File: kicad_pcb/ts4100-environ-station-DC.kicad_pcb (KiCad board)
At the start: 2 copper layers, 95 x 57.8 mm, 22 parts, among them CN1 Conn_02x08_Odd_Even, CN2 LXD-M4492C-LCD, CN3 Conn_01x02_MountingPin, CN4 Conn_01x04, Q1 DMN65D8LDW, U1 MS860702BA01-50

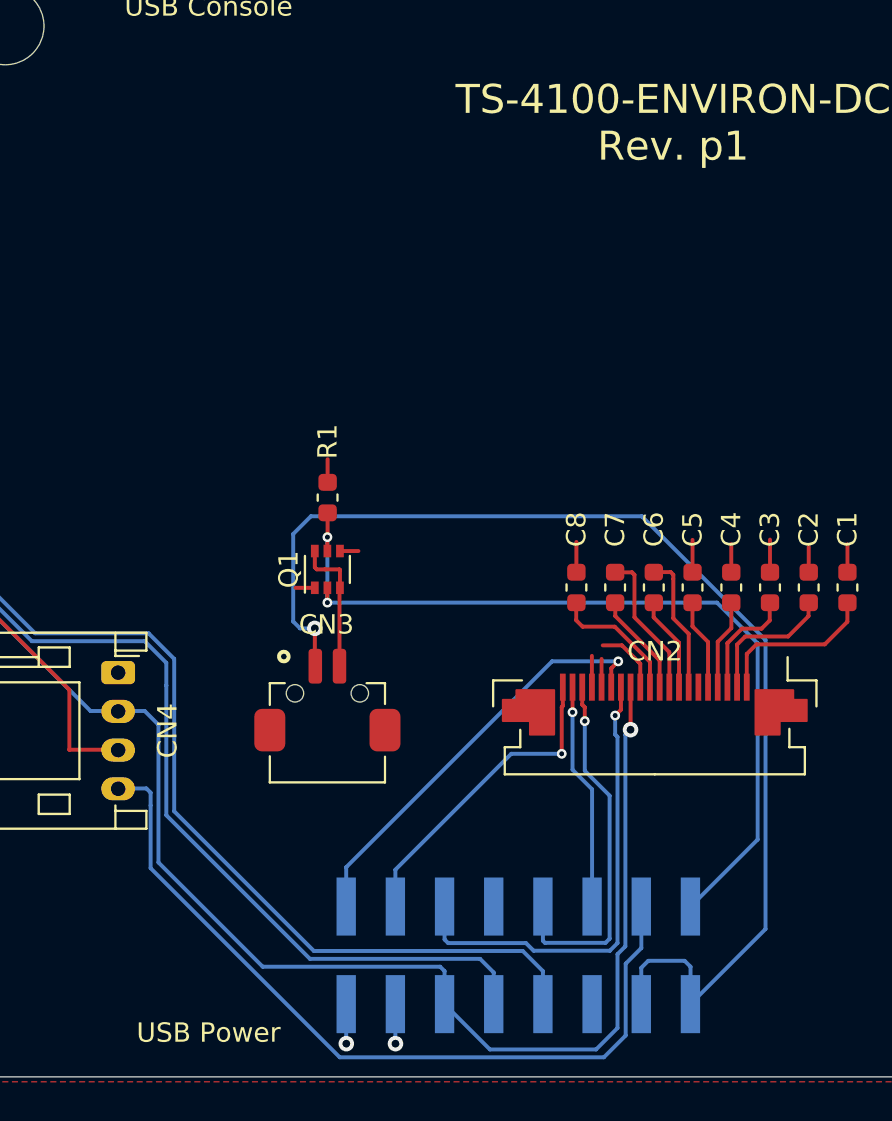
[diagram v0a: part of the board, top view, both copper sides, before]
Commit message: kicad_pcb: Bump to PCB rev p2
Runs LCD backlight on 3.3 V instead of 5 V, update silk, adds gnd
to backlight connector mounting pad footprints for mechanical
stability
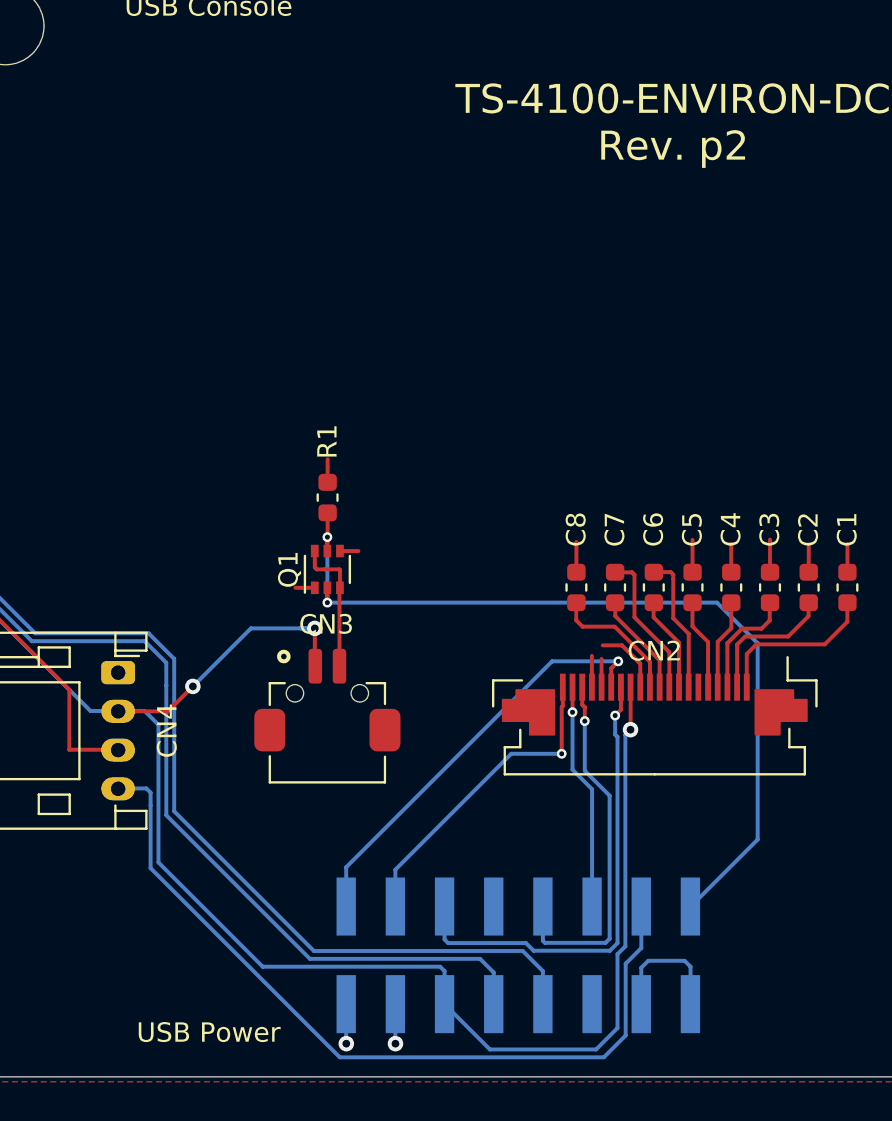
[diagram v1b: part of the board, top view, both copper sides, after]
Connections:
- CN3 pad 1: +5V -> +3V3
- CN3 pad MP: Net-(CN3-PadMP) -> GND
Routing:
- net +5V: track 62.1 -> 6.63 mm, vias 1 -> 0
- net +3V3: track 96.0 -> 110.5 mm, vias 2 -> 4
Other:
- board text added: "TS-4100-ENVIRON-DC Rev. p2"
- board text removed: "TS-4100-ENVIRON-DC Rev. p1"
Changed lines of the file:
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@@
     (thickness 1.6)
     (drawings 35)
-    (tracks 224)
+    (tracks 223)
     (zones 0)
     (modules 22)
-    (nets 35)
+    (nets 34)
   )
   (page A)
@@
     (mod_text_size 1 1)
     (mod_text_width 0.15)
-    (pad_size 1.7 1.7)
-    (pad_drill 1)
+    (pad_size 1.6 2.2)
+    (pad_drill 0)
     (pad_to_mask_clearance 0.05)
     (aux_axis_origin 0 0)
@@
   (net 31 "Net-(CN2-Pad21)")
   (net 32 "Net-(CN3-Pad2)")
-  (net 33 "Net-(CN3-PadMP)")
-  (net 34 "Net-(CN4-Pad1)")
+  (net 33 "Net-(CN4-Pad1)")
   (net_class Default "This is the default net class."
     (clearance 0.2032)
@@
     (add_net "Net-(CN2-Pad6)")
     (add_net "Net-(CN3-Pad2)")
-    (add_net "Net-(CN3-PadMP)")
     (add_net "Net-(CN4-Pad1)")
     (add_net "Net-(U1-Pad2)")
@@
     (fp_circle (center -2.25 -0.5) (end -2.15 -0.5) (layer F.SilkS) (width 0.5))
     (pad 1 smd roundrect (at -0.625 0) (size 0.7 1.8) (layers F.Cu F.Paste F.Mask) (roundrect_rratio 0.25)
-      (net 19 +5V))
+      (net 11 +3V3))
     (pad 2 smd roundrect (at 0.625 0) (size 0.7 1.8) (layers F.Cu F.Paste F.Mask) (roundrect_rratio 0.25)
       (net 32 "Net-(CN3-Pad2)"))
     (pad MP smd roundrect (at -2.975 3.3) (size 1.6 2.2) (layers F.Cu F.Paste F.Mask) (roundrect_rratio 0.25)
-      (net 33 "Net-(CN3-PadMP)"))
+      (net 1 GND))
     (pad MP smd roundrect (at 2.975 3.3) (size 1.6 2.2) (layers F.Cu F.Paste F.Mask) (roundrect_rratio 0.25)
-      (net 33 "Net-(CN3-PadMP)"))
+      (net 1 GND))
     (pad "" np_thru_hole circle (at 1.675 1.4) (size 0.9 0.9) (drill 0.9) (layers *.Cu *.Mask))
     (pad "" np_thru_hole circle (at -1.675 1.4) (size 0.9 0.9) (drill 0.9) (layers *.Cu *.Mask))
@@
     )
     (pad 1 thru_hole roundrect (at 0 0 270) (size 1.2 1.75) (drill 0.75) (layers *.Cu *.Mask) (roundrect_rratio 0.208333)
-      (net 34 "Net-(CN4-Pad1)"))
+      (net 33 "Net-(CN4-Pad1)"))
     (pad 2 thru_hole oval (at 2 0 270) (size 1.2 1.75) (drill 0.75) (layers *.Cu *.Mask)
       (net 11 +3V3))
@@
   (gr_line (start 101.092 99.568) (end 103.886 99.568) (layer Edge.Cuts) (width 0.05))
   (gr_line (start 101.092 92.3544) (end 101.092 99.568) (layer Edge.Cuts) (width 0.05))
-  (gr_text "TS-4100-ENVIRON-DC\nRev. p1" (at 148 89) (layer F.SilkS)
+  (gr_text "TS-4100-ENVIRON-DC\nRev. p2" (at 148 89) (layer F.SilkS)
     (effects (font (size 1.5 1.5) (thickness 0.15)))
   )
@@
   (segment (start 142.9893 114.6937) (end 142.9893 113.7982) (width 0.2032) (layer F.Cu) (net 10))
   (segment (start 120.7008 119.38) (end 119.38 119.38) (width 0.2032) (layer B.Cu) (net 11))
+  (segment (start 126.7968 132.588) (end 121.412 127.2032) (width 0.2032) (layer B.Cu) (net 11))
+  (segment (start 135.9612 132.588) (end 126.7968 132.588) (width 0.2032) (layer B.Cu) (net 11))
+  (segment (start 121.412 127.2032) (end 121.412 120.0912) (width 0.2032) (layer B.Cu) (net 11))
+  (segment (start 136.19 134.52) (end 136.19 132.8168) (width 0.2032) (layer B.Cu) (net 11))
+  (segment (start 136.19 132.8168) (end 135.9612 132.588) (width 0.2032) (layer B.Cu) (net 11))
   (segment (start 121.412 120.0912) (end 120.7008 119.38) (width 0.2032) (layer B.Cu) (net 11))
-  (segment (start 136.19 132.8168) (end 135.9612 132.588) (width 0.2032) (layer B.Cu) (net 11))
-  (segment (start 136.19 134.52) (end 136.19 132.8168) (width 0.2032) (layer B.Cu) (net 11))
-  (segment (start 121.412 127.2032) (end 121.412 120.0912) (width 0.2032) (layer B.Cu) (net 11))
-  (segment (start 135.9612 132.588) (end 126.7968 132.588) (width 0.2032) (layer B.Cu) (net 11))
-  (segment (start 126.7968 132.588) (end 121.412 127.2032) (width 0.2032) (layer B.Cu) (net 11))
   (segment (start 104.716 94.125) (end 102.0646 94.125) (width 0.2032) (layer F.Cu) (net 11))
   (segment (start 102.0572 93.0656) (end 102.0572 94.1832) (width 0.2032) (layer F.Cu) (net 11))
@@
   (segment (start 148.59 132.2832) (end 148.8948 132.588) (width 0.2032) (layer B.Cu) (net 19))
   (segment (start 148.8948 132.588) (end 148.8948 134.5184) (width 0.2032) (layer B.Cu) (net 19))
-  (segment (start 152.76831 115.714384) (end 146.375526 109.3216) (width 0.2032) (layer B.Cu) (net 19))
-  (segment (start 148.8948 134.5184) (end 152.768311 130.644889) (width 0.2032) (layer B.Cu) (net 19))
-  (segment (start 152.768311 130.644889) (end 152.76831 115.714384) (width 0.2032) (layer B.Cu) (net 19))
-  (segment (start 146.375526 109.3216) (end 129.286 109.3216) (width 0.2032) (layer B.Cu) (net 19))
-  (segment (start 128.3716 110.236) (end 128.3716 114.7572) (width 0.2032) (layer B.Cu) (net 19))
-  (via (at 129.4892 115.1128) (size 0.8) (drill 0.4) (layers F.Cu B.Cu) (net 19))
-  (segment (start 128.3716 114.7572) (end 128.7272 115.1128) (width 0.2032) (layer B.Cu) (net 19))
-  (segment (start 128.7272 115.1128) (end 129.4892 115.1128) (width 0.2032) (layer B.Cu) (net 19))
-  (segment (start 129.4892 115.1128) (end 129.4892 116.9416) (width 0.2032) (layer F.Cu) (net 19))
-  (segment (start 128.3716 110.236) (end 129.286 109.3216) (width 0.2032) (layer B.Cu) (net 19))
+  (segment (start 129.4892 115.1128) (end 129.4892 116.9416) (width 0.2032) (layer F.Cu) (net 11))
+  (segment (start 128.7272 115.1128) (end 129.4892 115.1128) (width 0.2032) (layer B.Cu) (net 11))
+  (via (at 129.4892 115.1128) (size 0.8) (drill 0.4) (layers F.Cu B.Cu) (net 11))
+  (segment (start 119.3292 119.3988) (end 121.9012 119.3988) (width 0.2032) (layer F.Cu) (net 11))
+  (segment (start 121.9012 119.3988) (end 123.19 118.11) (width 0.2032) (layer F.Cu) (net 11))
+  (segment (start 129.4892 115.1128) (end 126.1872 115.1128) (width 0.2032) (layer B.Cu) (net 11))
+  (segment (start 126.1872 115.1128) (end 123.19 118.11) (width 0.2032) (layer B.Cu) (net 11))
+  (segment (start 123.19 118.11) (end 123.19 118.11) (width 0.2032) (layer F.Cu) (net 11))
+  (via (at 123.19 118.11) (size 0.8) (drill 0.4) (layers F.Cu B.Cu) (net 11))
   (segment (start 119.38 123.38) (end 120.7892 123.38) (width 0.2032) (layer B.Cu) (net 20))
   (segment (start 120.7892 123.38) (end 121.00559 123.59639) (width 0.2032) (layer B.Cu) (net 20))
